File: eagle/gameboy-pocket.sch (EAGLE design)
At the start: 33 parts, among them J1 AUDIO_JACK_3.5MM_PTH, U1 LM4875

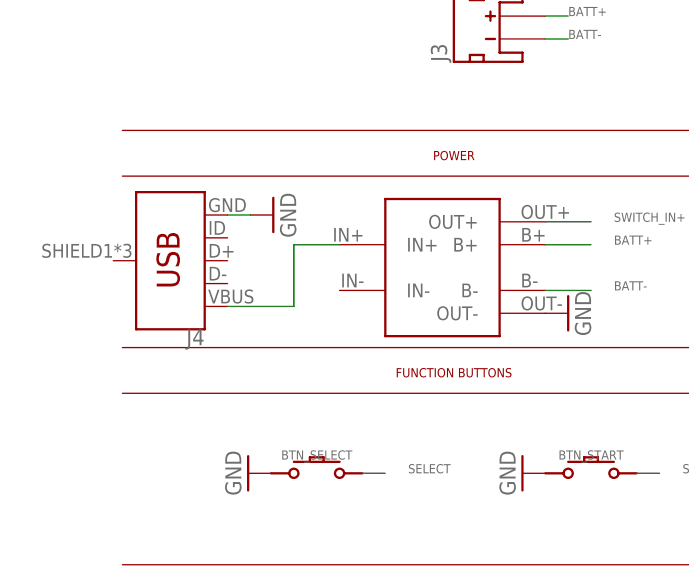
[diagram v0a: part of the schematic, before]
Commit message: routed main components and usb for charging
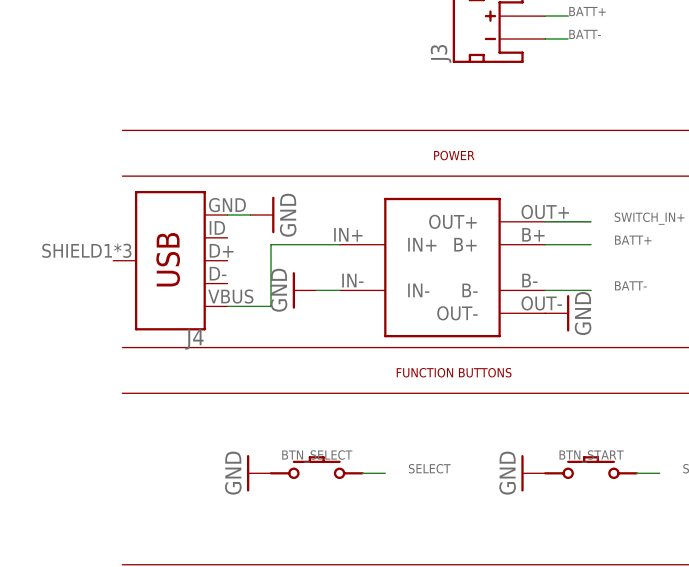
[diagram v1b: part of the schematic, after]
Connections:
- net N$1 renamed VUSB
- net GND: now also POWER1.IN-
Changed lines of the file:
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@@
 <part name="J4" library="SparkFun-Connectors" library_urn="urn:adsk.eagle:library:513" deviceset="USB_MICRO-B" device="_FEMALE-SMT" package3d_urn="urn:adsk.eagle:package:38238/1"/>
 <part name="GND24" library="supply1" library_urn="urn:adsk.eagle:library:371" deviceset="GND" device=""/>
+<part name="GND26" library="supply1" library_urn="urn:adsk.eagle:library:371" deviceset="GND" device=""/>
 </parts>
 <sheets>
@@
 <instance part="J4" gate="G$1" x="10.414" y="109.982" rot="R180"/>
 <instance part="GND24" gate="1" x="20.574" y="115.062" rot="R90"/>
+<instance part="GND26" gate="1" x="22.86" y="106.68" rot="R270"/>
 </instances>
 <busses>
@@
 <wire x1="18.034" y1="115.062" x2="15.494" y2="115.062" width="0.1524" layer="91"/>
 </segment>
+<segment>
+<pinref part="POWER1" gate="G$1" pin="IN-"/>
+<pinref part="GND26" gate="1" pin="GND"/>
+<wire x1="25.4" y1="106.68" x2="27.94" y2="106.68" width="0.1524" layer="91"/>
+</segment>
 </net>
 <net name="RESET" class="0">
@@
 </segment>
 </net>
-<net name="N$1" class="0">
+<net name="VUSB" class="0">
 <segment>
 <pinref part="J4" gate="G$1" pin="VBUS"/>
-<wire x1="15.494" y1="104.902" x2="22.86" y2="104.902" width="0.1524" layer="91"/>
-<wire x1="22.86" y1="104.902" x2="22.86" y2="111.76" width="0.1524" layer="91"/>
+<wire x1="15.494" y1="104.902" x2="20.32" y2="104.902" width="0.1524" layer="91"/>
+<wire x1="20.32" y1="104.902" x2="20.32" y2="111.76" width="0.1524" layer="91"/>
 <pinref part="POWER1" gate="G$1" pin="IN+"/>
-<wire x1="22.86" y1="111.76" x2="27.94" y2="111.76" width="0.1524" layer="91"/>
-</segment>
-</net>
+<wire x1="20.32" y1="111.76" x2="27.94" y2="111.76" width="0.1524" layer="91"/>
+</segment>
+</net>
